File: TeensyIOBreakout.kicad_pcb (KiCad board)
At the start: 2 copper layers, 50 x 42.5 mm, 13 parts, among them J1 Conn_01x14_Male, J2 Conn_01x14_Male, J3 Conn_01x14_Male, J4 Conn_01x14_Male, J5 Conn_01x03_Male, J6 Conn_01x05_Male, J7 Conn_01x02_Male, U1 Teensy3.2

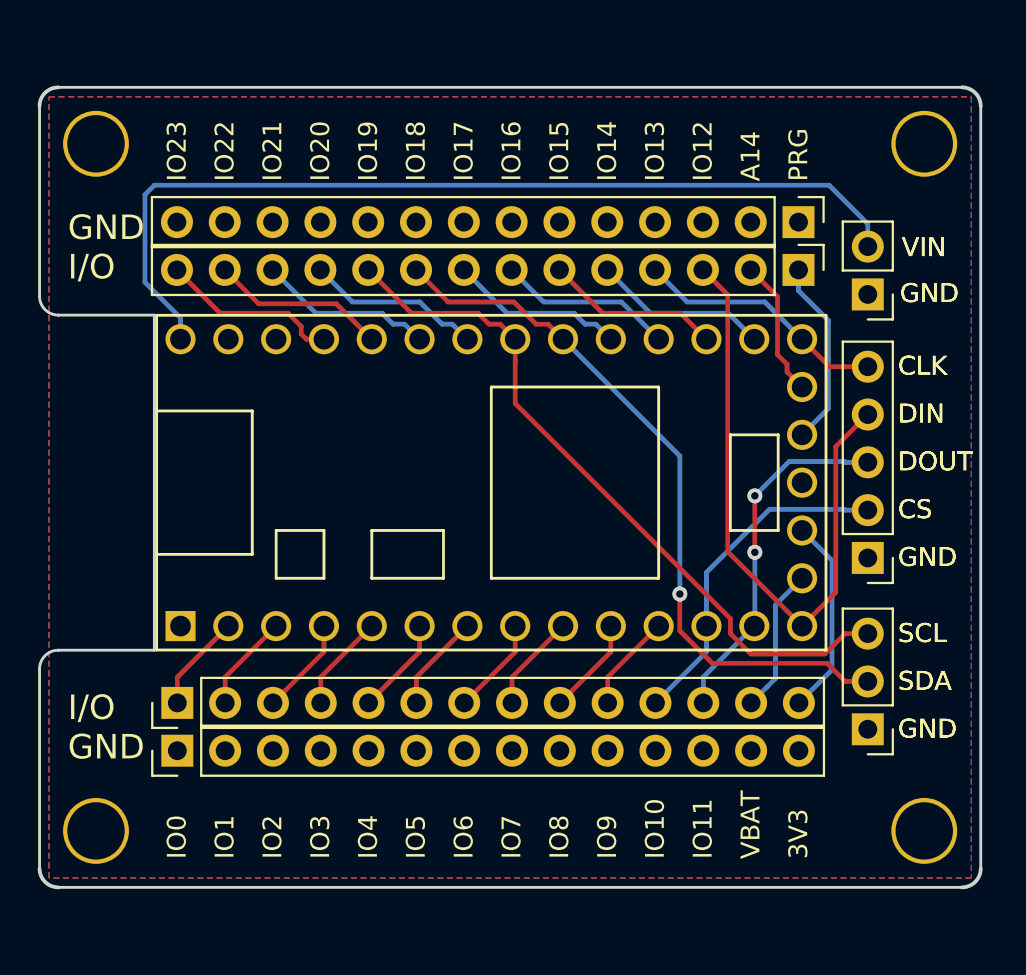
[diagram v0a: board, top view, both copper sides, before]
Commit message: Added 3V3 rail, moved I2C/SPI/VIN headers
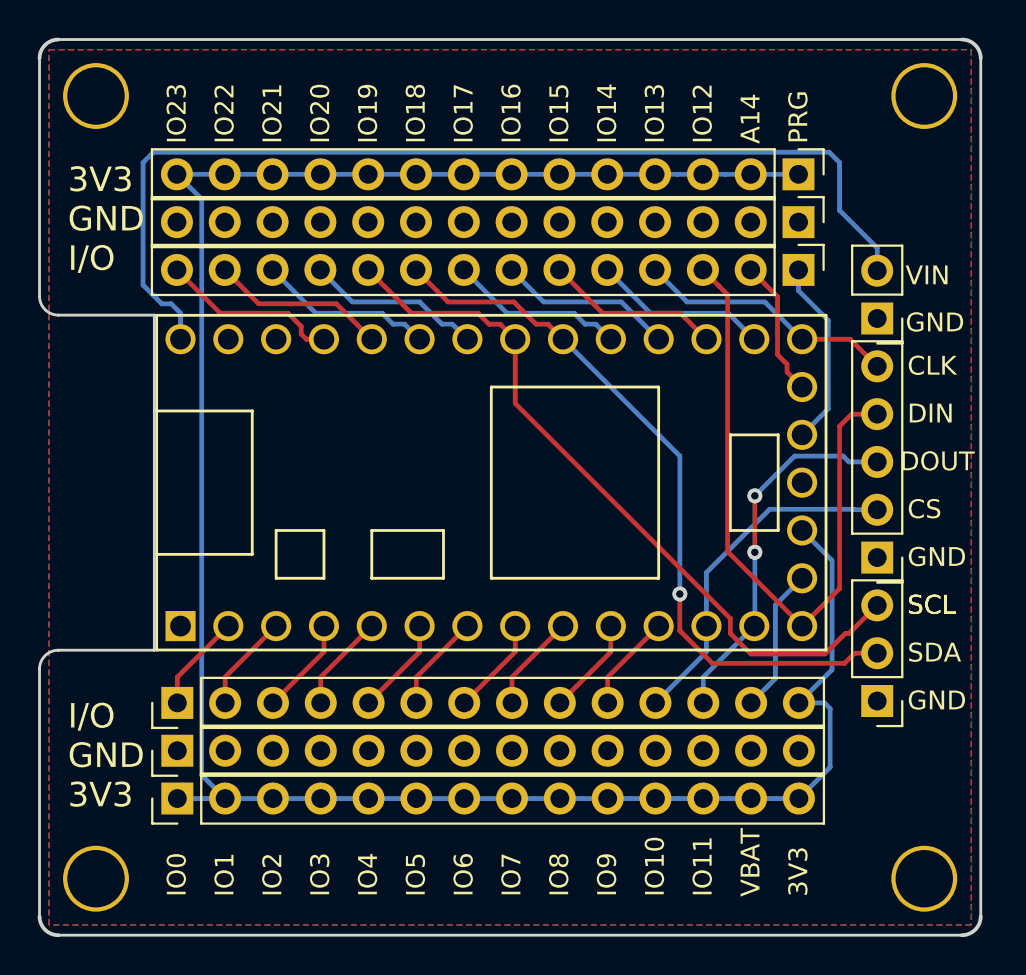
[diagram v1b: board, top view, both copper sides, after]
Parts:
- added J8: Conn_01x14_Male, Pin_Headers:Pin_Header_Straight_1x14_Pitch2.54mm, F.Cu at (113.3, 55.3)
- added J9: Conn_01x14_Male, Pin_Headers:Pin_Header_Straight_1x14_Pitch2.54mm, F.Cu at (146.3, 22.1)
- moved REF** 2.54 mm to (153.0, 59.5)
- moved REF** 2.54 mm to (153.0, 18.0)
- moved REF** 2.54 mm to (109.0, 18.0)
- moved REF** 2.54 mm to (109.0, 59.5)
- moved J5 1.58 mm to (150.5, 50.1)
- moved J7 1.37 mm to (150.5, 29.8)
- moved J6 0.50 mm to (150.5, 42.5)
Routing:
- net 3V3: track 10.5 -> 118.1 mm
- net Vin: track 49.1 -> 54.5 mm
- net IO_19: track 37.9 -> 39.0 mm
- net IO_12: track 33.8 -> 34.8 mm
- net IO_11: track 18.9 -> 19.6 mm
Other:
- board size 50 x 42.5 mm -> 50 x 47.6 mm
- board text added: "3V3 GND I/O"
- board text added: "I/O GND 3V3"
- board text removed: "GND I/O"
- board text removed: "I/O GND"
